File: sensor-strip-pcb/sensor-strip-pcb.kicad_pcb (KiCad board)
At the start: 2 copper layers, 12 parts, among them J1 LED_Strip, J10 Arduino_Sensor_Power_Input, J2 Left_Colour_Sensor, J3 Right_Colour_Sensor, J4 Red_Right_Detect_Pin, J5 Blue_Right_Detect_Pin, J6 Red_Left_Detect_Pin, J7 Blue_Left_Detect_Pin, J8 Right_Enable_Pin, J9 Left_Enable_Pin

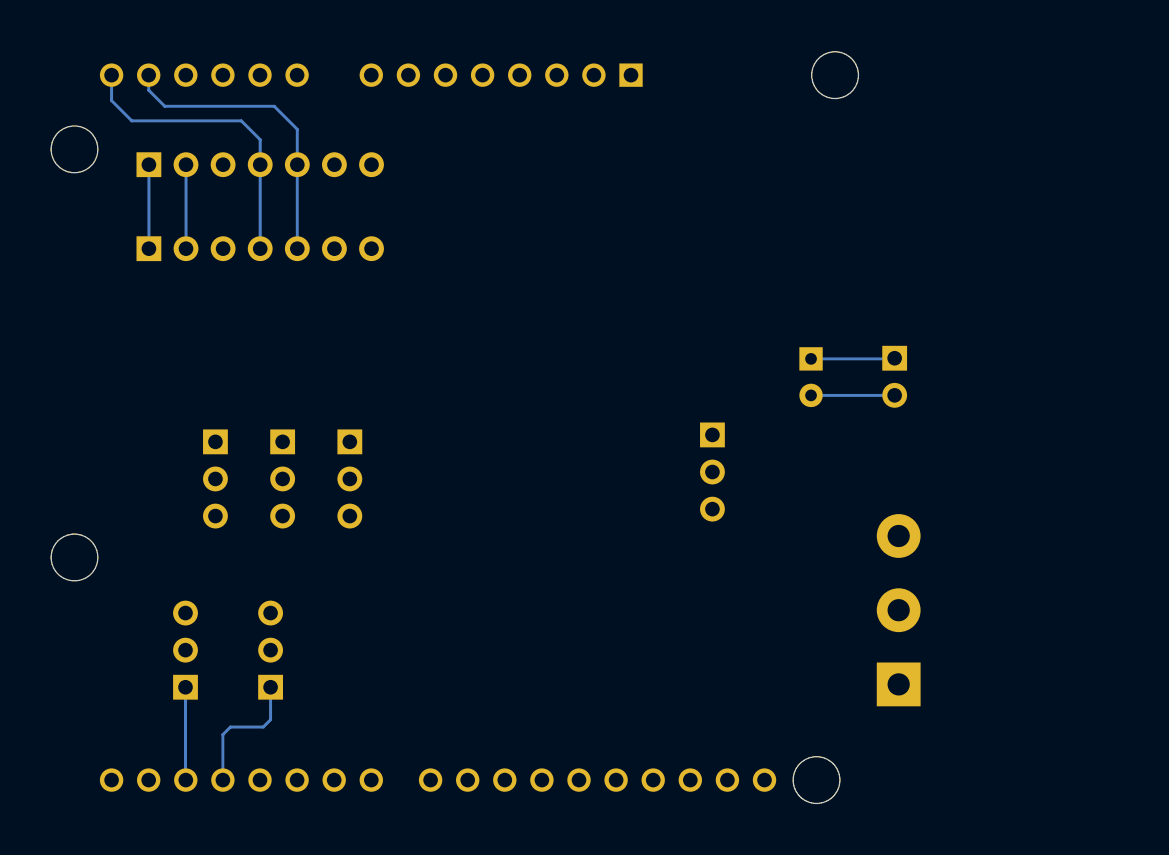
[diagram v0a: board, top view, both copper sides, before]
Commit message: Updated layout and traces, needs I2C MUX
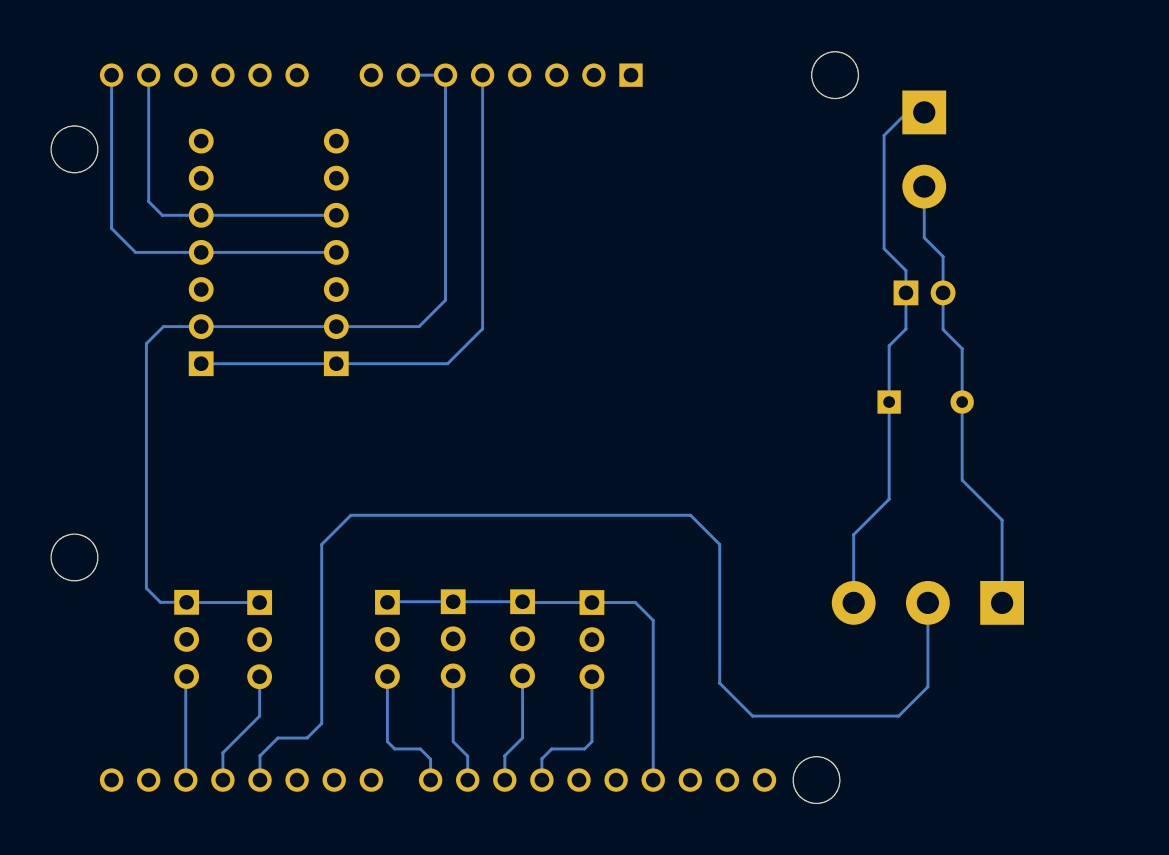
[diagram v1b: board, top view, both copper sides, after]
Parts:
- added J11: Arduino_Strip_Vin_Terminal, TerminalBlock:TerminalBlock_bornier-2_P5.08mm, B.Cu at (114.2, 52.9)
- C1: value 10uF -> 100uf; footprint Capacitor_THT:CP_Radial_D5.0mm_P2.50mm -> Capacitor_THT:CP_Radial_D8.0mm_P5.00mm
- J10: value Arduino_Sensor_Power_Input -> Arduino_Strip_Vin_Header
- J2, J3: footprint Connector_PinSocket_2.54mm:PinSocket_1x07_P2.54mm_Vertical -> Connector_PinHeader_2.54mm:PinHeader_1x07_P2.54mm_Vertical
- J4, J5, J6, J7, J8, J9: footprint Connector_PinSocket_2.54mm:PinSocket_1x03_P2.54mm_Vertical -> Connector_PinHeader_2.54mm:PinHeader_1x03_P2.54mm_Vertical
- moved J6 23.7 mm to (86.8, 86.4)
- moved J5 16.0 mm to (82.0, 86.4)
- moved J2 15.1 mm to (74.0, 70.1), turned to 0 degrees
- moved J7 14.1 mm to (91.5, 86.5)
- moved J3 14.1 mm to (64.8, 70.1), turned to 0 degrees
- moved J4 11.3 mm to (77.5, 86.5)
- moved J1 9.01 mm to (119.6, 86.5), turned to 180 degrees
- moved C1 6.11 mm to (111.8, 72.8), turned to 0 degrees
- moved J9 5.85 mm to (68.8, 86.5), turned to 180 degrees
- moved J8 5.82 mm to (63.8, 86.5), turned to 180 degrees
- moved J10 4.54 mm to (113.0, 65.3), turned to -90 degrees
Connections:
- C1 pad 1: Net-(J10-Pin_1) -> 5v_EXT
- C1 pad 2: GND -> GND_EXT
- J1 pad 1: 5v -> GND_EXT
- J1 pad 3: GND -> 5v_EXT
- J10 pad 1: Net-(J10-Pin_1) -> 5v_EXT
- J10 pad 2: GND -> GND_EXT
- J4 pad 1: RR_PIN -> GND
- J4 pad 2: 5v -> unconnected-(J4-Pin_2-Pad2)
- J4 pad 3: GND -> RR_PIN
- J5 pad 1: BR_PIN -> GND
- J5 pad 2: 5v -> unconnected-(J5-Pin_2-Pad2)
- J5 pad 3: GND -> BR_PIN
- J6 pad 1: RL_PIN -> GND
- J6 pad 2: 5v -> unconnected-(J6-Pin_2-Pad2)
- J6 pad 3: GND -> RL_PIN
- J7 pad 1: BL_PIN -> GND
- J7 pad 2: 5v -> unconnected-(J7-Pin_2-Pad2)
- J7 pad 3: GND -> BL_PIN
- J8 pad 1: REN_PIN -> GND
- J8 pad 2: 5v -> unconnected-(J8-Pin_2-Pad2)
- J8 pad 3: GND -> REN_PIN
- J9 pad 1: LEN_PIN -> GND
- J9 pad 2: 5v -> unconnected-(J9-Pin_2-Pad2)
- J9 pad 3: GND -> LEN_PIN
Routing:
- net GND: track 11.5 -> 94.2 mm
- net NEO_DATA: track 0.00 -> 79.2 mm
- net 5v_EXT: track 0.00 -> 37.5 mm
- net 5v: track 5.75 -> 37.6 mm
- net GND_EXT: track 0.00 -> 30.7 mm
- net BL_PIN: track 0.00 -> 9.81 mm
- net RR_PIN: track 0.00 -> 9.34 mm
- net RL_PIN: track 0.00 -> 7.63 mm
- net BR_PIN: track 0.00 -> 7.54 mm
- net SCL: track 20.5 -> 26.6 mm
- net Net-(J10-Pin_1): track 5.74 -> 0.00 mm
- net SDA: track 20.5 -> 21.9 mm
- net LEN_PIN: track 9.03 -> 8.12 mm
- net REN_PIN: track 6.36 -> 7.11 mm
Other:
- board text added: "BLU_L Det."
- board text added: "BLU_R Det."
- board text added: "L En."
- board text added: "R En."
- board text added: "RED_L Det."
- board text added: "RED_R Det."

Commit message: Finalized layout and trace routing
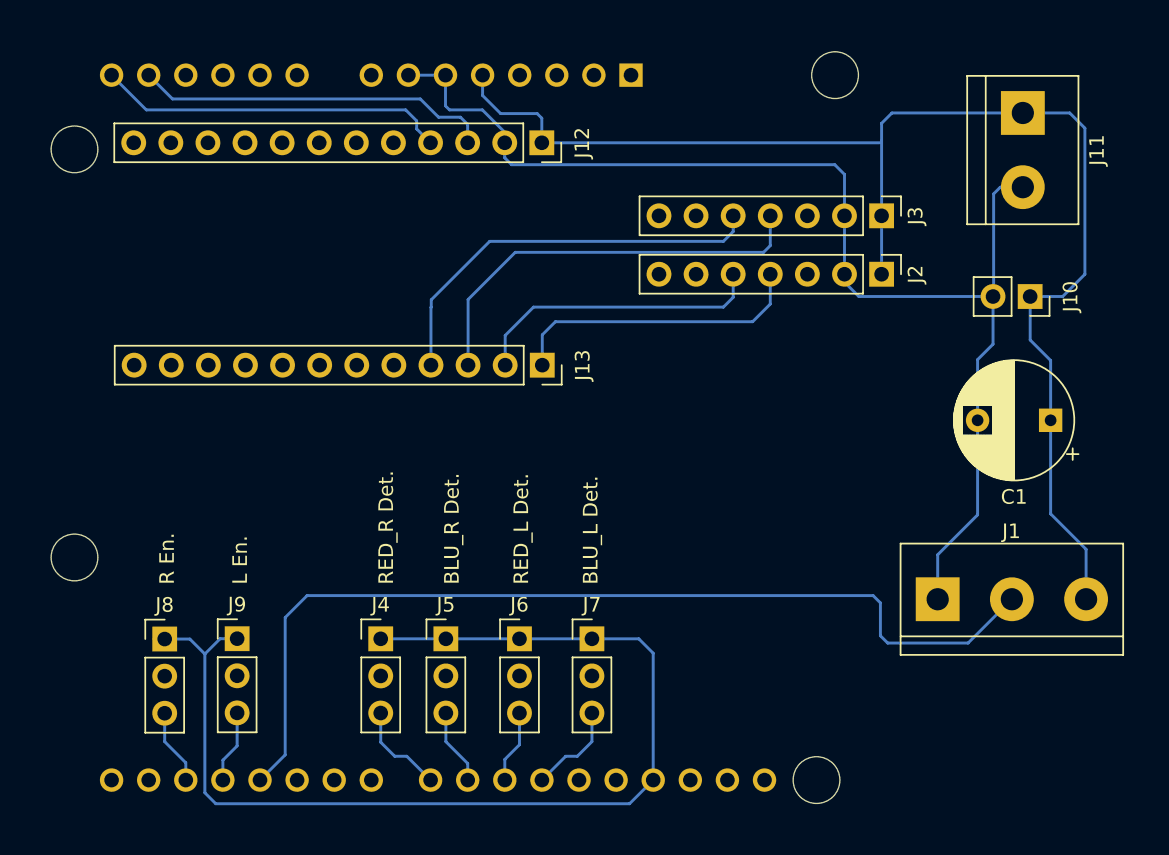
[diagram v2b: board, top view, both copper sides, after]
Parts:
- added J12: TCA9548A_Left_Socket, Connector_PinSocket_2.54mm:PinSocket_1x12_P2.54mm_Vertical, F.Cu at (88.1, 55.0)
- added J13: TCA9548A_Left_Socket, Connector_PinSocket_2.54mm:PinSocket_1x12_P2.54mm_Vertical, F.Cu at (88.1, 70.2)
- C1, J1, J10, J11, J2, J3, J4, J5, J6, J7, J8, J9: moved to F.Cu
- moved J3 47.7 mm to (111.3, 60.0), turned to -90 degrees
- moved J2 37.8 mm to (111.3, 64.0), turned to -90 degrees
- moved C1 11.1 mm to (122.9, 74.0), turned to 180 degrees
- moved J10 8.50 mm to (121.5, 65.5)
- moved J11 6.75 mm to (121.0, 53.0)
- moved J1 4.42 mm to (115.2, 86.2), turned to 0 degrees
- moved J8 2.93 mm to (62.2, 89.0), turned to 0 degrees
- moved J9 2.92 mm to (67.2, 89.0), turned to 0 degrees
- moved J5 2.59 mm to (81.5, 89.0), turned to 0 degrees
- moved J6 2.55 mm to (86.5, 89.0), turned to 0 degrees
- moved J4 2.54 mm to (77.0, 89.0), turned to 0 degrees
- moved J7 2.48 mm to (91.5, 89.0), turned to 0 degrees
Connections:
- C1 pad 1: 5v_EXT -> 5v
- C1 pad 2: GND_EXT -> GND
- J1 pad 1: GND_EXT -> GND
- J1 pad 3: 5v_EXT -> 5v
- J10 pad 1: 5v_EXT -> 5v
- J10 pad 2: GND_EXT -> GND
- J11 pad 1: 5v_EXT -> 5v
- J11 pad 2: GND_EXT -> GND
- J2 pad 4: SCL -> SCL_7
- J2 pad 5: SDA -> SDA_7
- J3 pad 4: SCL -> SCL_6
- J3 pad 5: SDA -> SDA_6
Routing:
- net GND: track 94.2 -> 159.2 mm
- net 5v: track 37.6 -> 92.6 mm
- net 5v_EXT: track 37.5 -> 0.00 mm
- net GND_EXT: track 30.7 -> 0.00 mm
- net SCL_6: track 0.00 -> 28.8 mm
- net SDA_6: track 0.00 -> 28.2 mm
- net SCL_7: track 0.00 -> 20.6 mm
- net SDA_7: track 0.00 -> 20.3 mm
- net NEO_DATA: track 79.2 -> 66.1 mm
- net BL_PIN: track 9.81 -> 6.47 mm
- net LEN_PIN: track 8.12 -> 5.00 mm
- net RR_PIN: track 9.34 -> 6.49 mm
- net RL_PIN: track 7.63 -> 5.01 mm
- net SDA: track 21.9 -> 24.5 mm
- net SCL: track 26.6 -> 24.1 mm
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
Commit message: Finished silkscreen, finalized v1
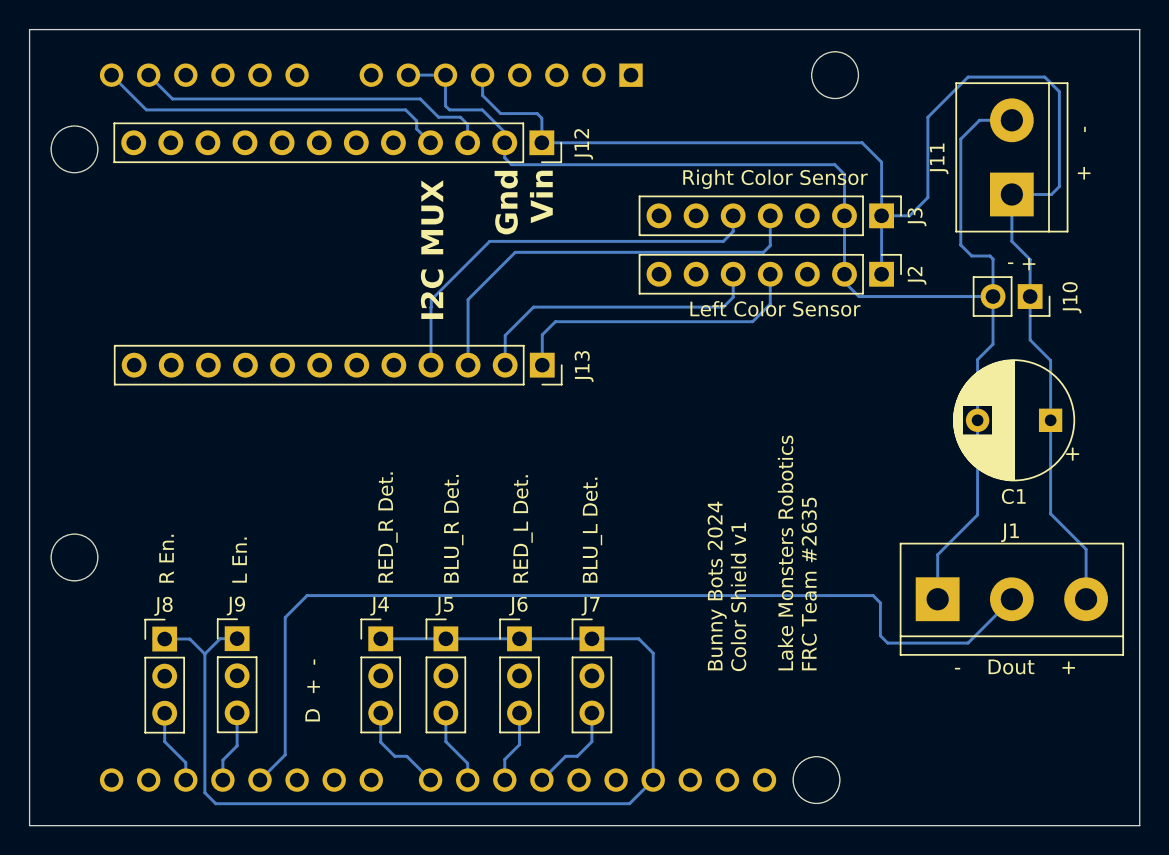
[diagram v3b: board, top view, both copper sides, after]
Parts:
- J11: value Arduino_Strip_Vin_Terminal -> Arduino_Vin_Terminal
- J13: value TCA9548A_Left_Socket -> TCA9548A_Right_Socket
- moved J11 5.63 mm to (120.2, 58.5), turned to 90 degrees
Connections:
- J12 pad 10: SCL_0 -> unconnected-(J12-Pin_10-Pad10)
- J12 pad 11: SDA_1 -> unconnected-(J12-Pin_11-Pad11)
- J12 pad 12: SCL_1 -> unconnected-(J12-Pin_12-Pad12)
- J12 pad 9: SDA_0 -> unconnected-(J12-Pin_9-Pad9)
- J13 pad 11: SCL_2 -> unconnected-(J13-Pin_11-Pad11)
- J13 pad 12: SDA_2 -> unconnected-(J13-Pin_12-Pad12)
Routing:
- net GND: track 159.2 -> 166.4 mm
- net 5v: track 92.6 -> 98.8 mm
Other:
- board outline added: 76 x 54.5 mm
- board text added: "+ -"
- board text added: "- Dout +"
- board text added: "Bunny Bots 2024 Color Shield v1 Lake Monsters Robotics FRC Team #2635"
- board text added: "D + -"
- board text added: "Gnd Vin"
- board text added: "I2C MUX"
- board text added: "Left Color Sensor"
- board text added: "Right Color Sensor"
